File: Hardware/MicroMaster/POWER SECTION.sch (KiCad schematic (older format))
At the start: 16 parts

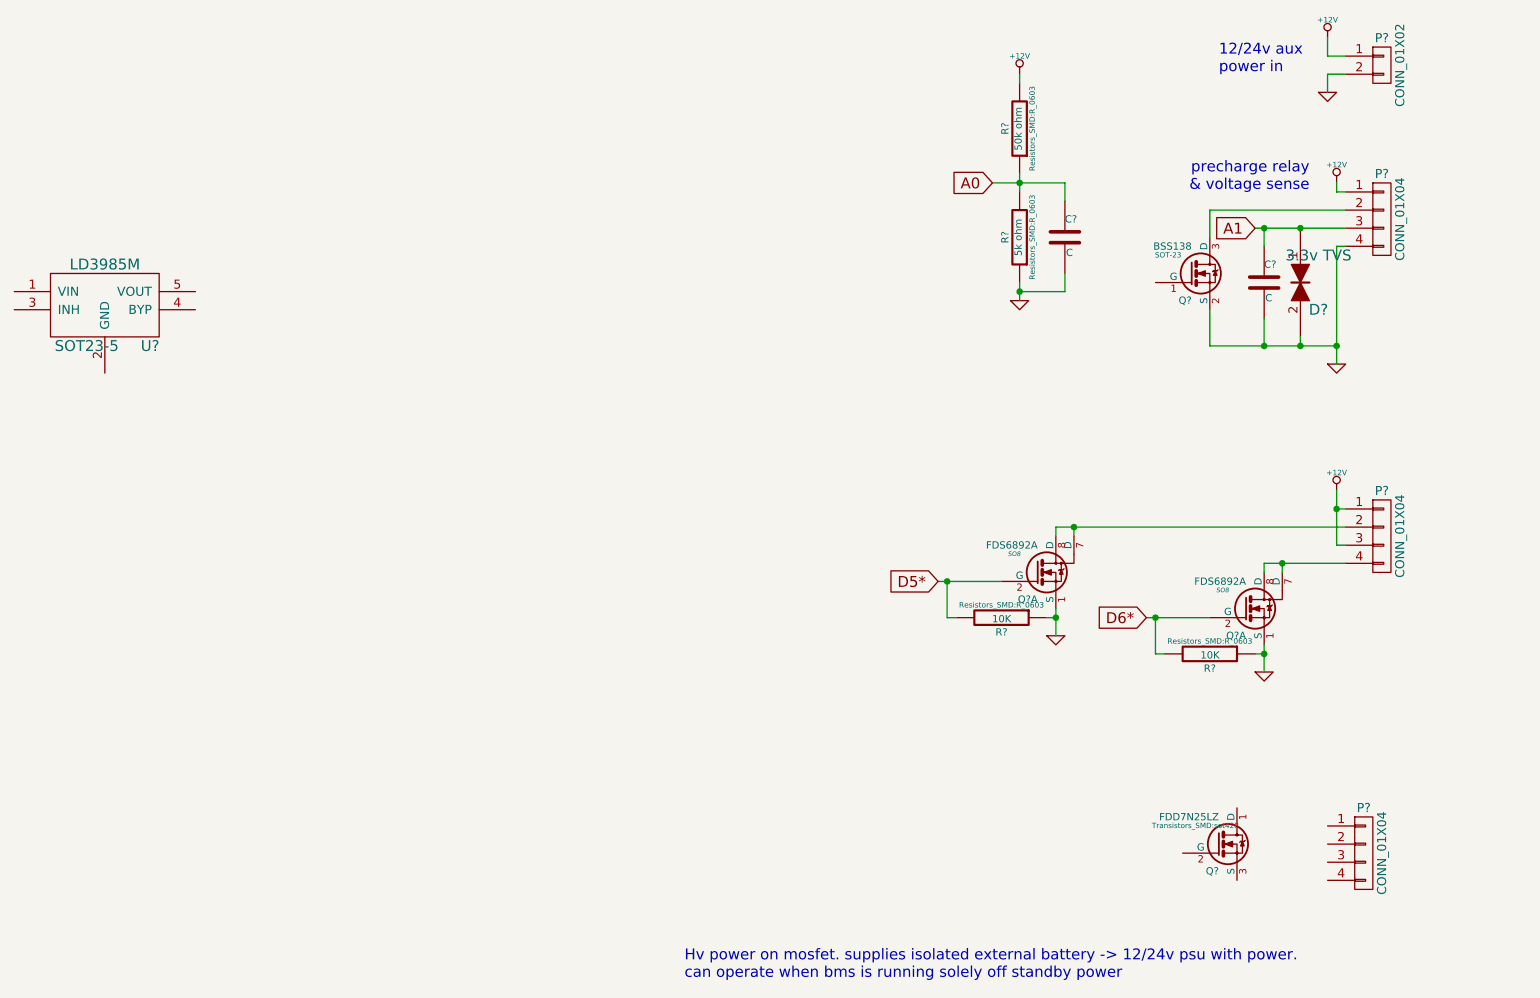
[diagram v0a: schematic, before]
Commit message: Fixed test code and schematic
Fixed a problem in the code that caused it to hang. spi now appears to
be working porperly with a logic analyzer.  I also finished up some
stuff with the micromaster schematic. It is now ready to be laied out on
a pcb
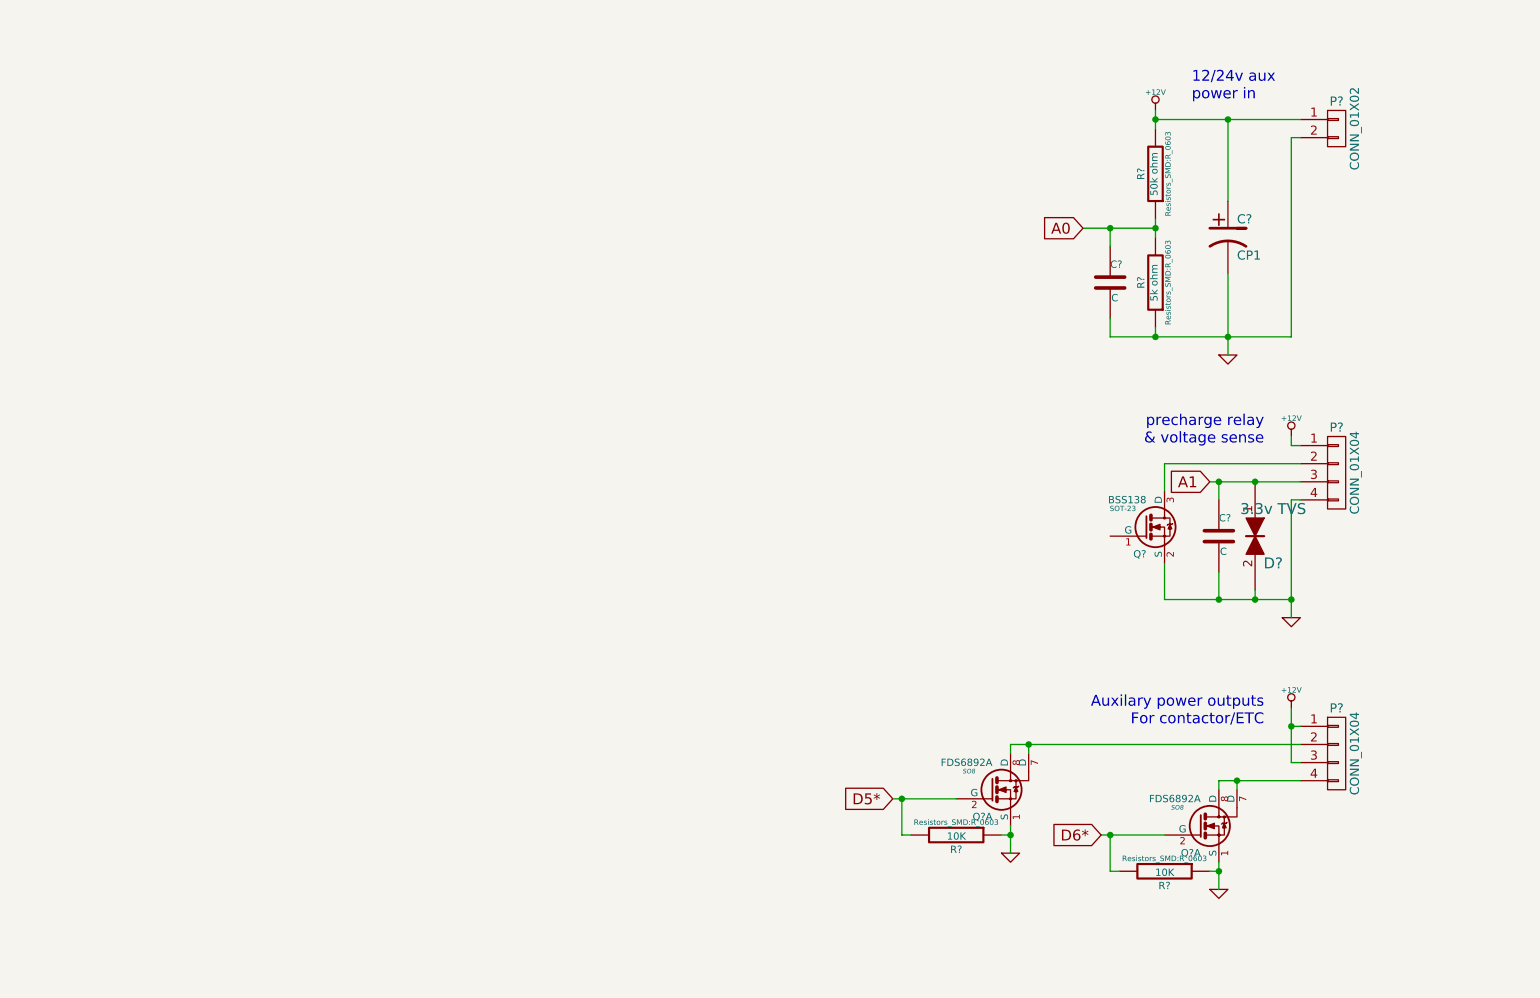
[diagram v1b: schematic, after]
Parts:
- removed P?: CONN_01X04, symbol CONN_01X04
- removed Q?: FDD7N25LZ, Transistors_SMD:sot428, symbol BS107
- removed U?: LD3985M, SOT23-5, symbol LD3985M
- added C?: CP1, symbol CP1
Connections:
- net +12V: now also C?.1
- net GND: now also C?.2
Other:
- note added: "Auxilary power outputs\nFor contactor/ETC"
- note removed: "Hv power on mosfet. supplies isolated external battery -> 12/24v psu with power.\ncan operate when bms is running solely off standby power"
- moved on the sheet: C?, D?, P?, Q?, Q?A, R?
